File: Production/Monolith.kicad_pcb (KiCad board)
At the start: 2 copper layers, 5.7 x 10.2 mm, 276 parts, among them J102 Cell 1 NTC wires, J105 Cell 2 NTC wires, J106 Cell 3 NTC wires, J107 Cell 4 NTC wires, J108 PACK- (CELL_N), J109 CELL1 tap, J110 CELL2 tap, J111 CELL3 tap, J112 PACK+ (CELL_P_RAW), J301 TC2030-NL, J401 TYPE-C 16PCB1.6 IP68, J501 TYPE-C 16PCB1.6 IP68, Q101 AGM404AP1, Q102 AGM404AP1, Q103 AO3400A, Q104 AO3400A, Q401 PGQ04N070, Q402 PGQ04N070, Q403 AO3401A, Q404 AO3401A, Q405 AO3400A, Q406 AO3400A, Q407 PGQ04N070, Q408 PGQ04N070, Q501 PGQ04N070, Q502 PGQ04N070, Q503 AO3401A, Q504 AO3401A, Q505 AO3400A, Q506 AO3400A, Q507 PGQ04N070, Q508 PGQ04N070, U101 BQ40Z50RSMR-R2, U102 BQ294700DSGR, U204 TPS62177DQCR, U301 CC2340R5MODA, U401 TPS25751DREFR, U402 M24512-DFMC6TG, U403 BQ25756RRVR, U404 TPS62933DRLR, U405 TPD4S201TRGRRQ1, U501 TPS25751DREFR, U502 M24512-DFMC6TG, U503 BQ25756RRVR, U504 TPS62933DRLR, U505 TPD4S201TRGRRQ1

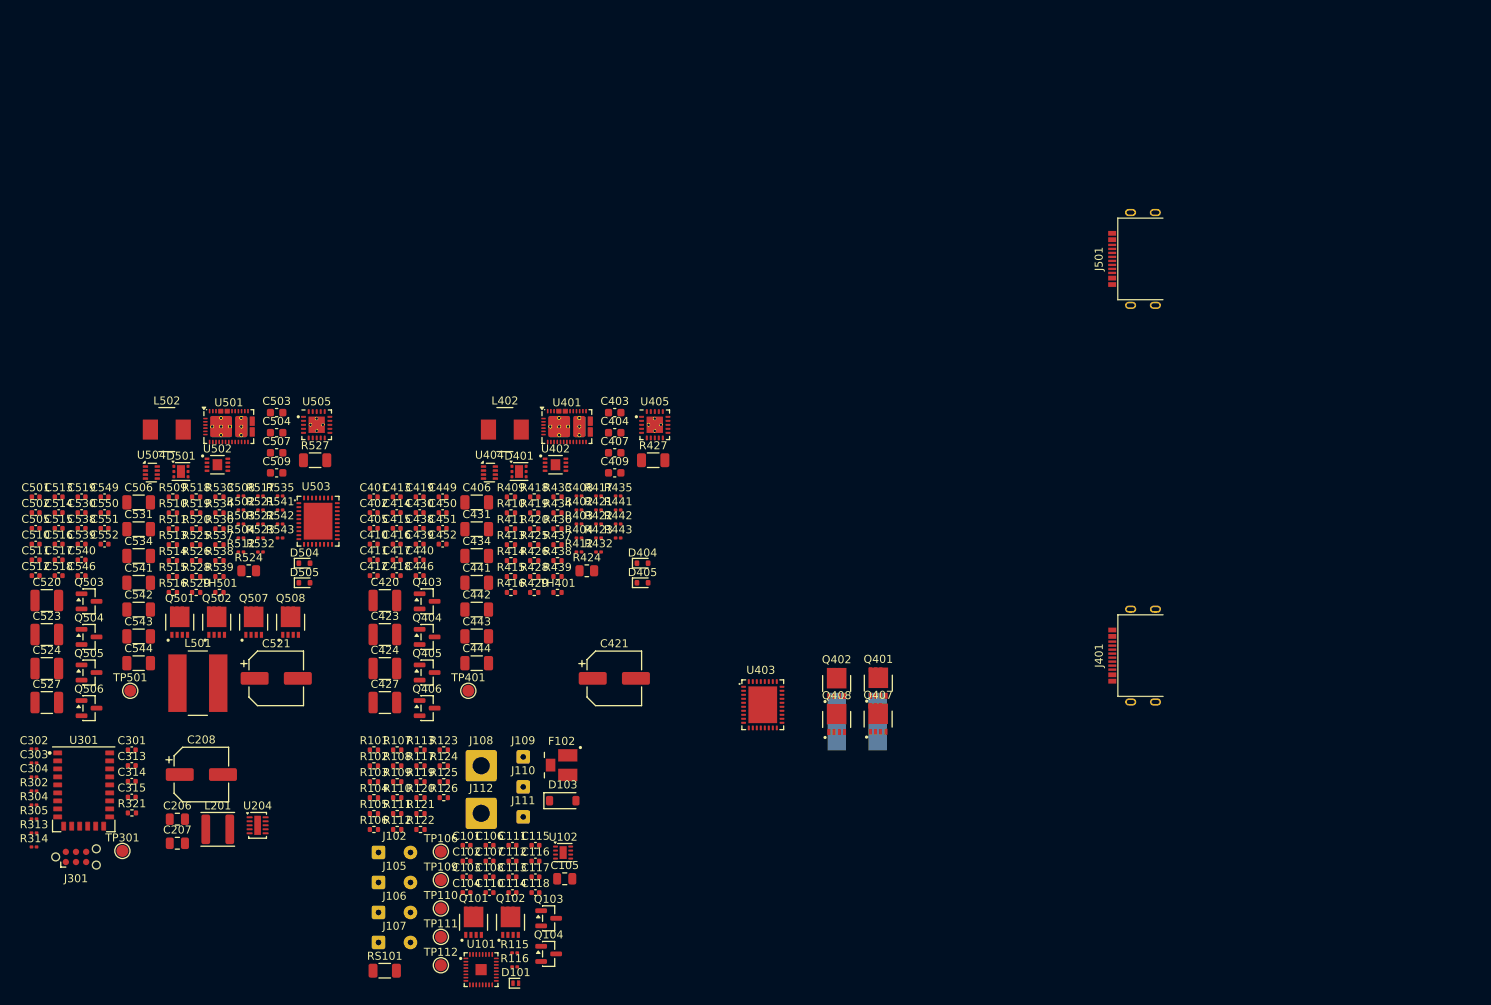
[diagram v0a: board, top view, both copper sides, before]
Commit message: Production board: 6-layer 0.8 mm stack-up, top-cap outline, pour plan
tools/make_board.py patches Monolith.kicad_pcb (footprints untouched): 6 layers,
0.8 mm, 2 oz outer / 0.5 oz inner, ENIG, filled vias; 40.5 mm R9.35 outline
from mechanical/monolith_parts.py (the bottom DXF is the end board). Via
minimum 0.35/0.2 for fan-out. J401/J501 -> TYPE-C 16PCB0.8 IP68 (C55629727).
Pour plan in Production/README.md.

Co-Authored-By: Claude Opus 5.5 <noreply@anthropic.com>
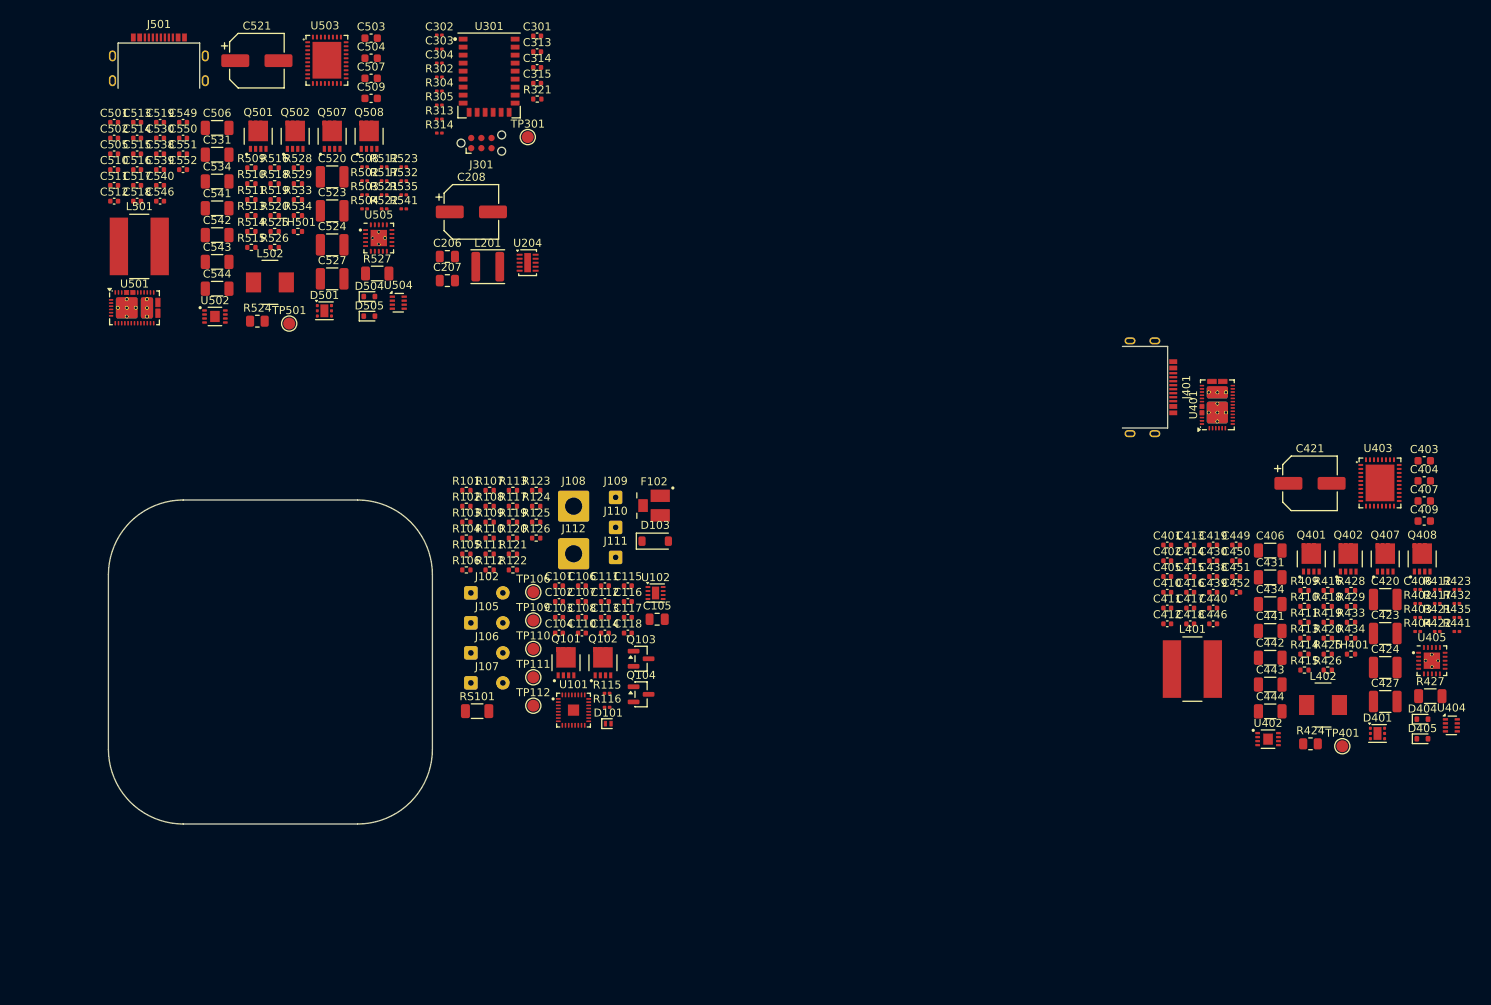
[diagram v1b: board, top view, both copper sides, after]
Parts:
- removed Q403, Q404, Q503, Q504: AO3401A, Package_TO_SOT_SMD:SOT-23
- removed Q405, Q406, Q505, Q506: AO3400A, Package_TO_SOT_SMD:SOT-23
- removed R436, R437, R536, R537: 100k, Resistor_SMD:R_0402_1005Metric
- removed R438, R439, R538, R539: 1M, Resistor_SMD:R_0402_1005Metric
- removed R442, R443, R542, R543: 100k, Resistor_SMD:R_0201_0603Metric
- L401: moved to F.Cu
- moved J501 127.3 mm to (86.1, 28.3), turned to 0 degrees
- moved C420 125.0 mm to (239.4, 92.2)
- moved C423 125.0 mm to (239.4, 96.4)
- moved C424 125.0 mm to (239.4, 100.7)
- moved C427 125.0 mm to (239.4, 104.9)
- moved U404 124.3 mm to (247.6, 107.9)
- moved D401 112.2 mm to (238.4, 108.9)
- moved TP401 109.5 mm to (234.0, 110.5)
- moved L402 107.9 mm to (231.6, 105.4)
- moved R423 107.5 mm to (248.3, 90.9)
- moved R432 107.5 mm to (248.3, 92.7)
- moved R412 107.4 mm to (245.9, 90.9)
- moved R435 105.9 mm to (248.3, 94.4)
- moved R441 105.9 mm to (248.3, 96.2)
- moved R417 105.7 mm to (245.9, 92.7)
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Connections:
- U401 pad 26: /USB Port 1/SBU1_SNS -> GND
- U401 pad 27: /USB Port 1/SBU2_SNS -> GND
- U401 pad 36: /USB Port 1/LIQ_PD -> GND
- U401 pad 37: /USB Port 1/LIQ_PU -> GND
- U405 pad 14: /USB Port 1/SBU2_SNS -> unconnected-(U405-SBU2-Pad14)
- U405 pad 15: /USB Port 1/SBU1_SNS -> unconnected-(U405-SBU1-Pad15)
- U501 pad 26: /USB Port 2/SBU1_SNS -> GND
- U501 pad 27: /USB Port 2/SBU2_SNS -> GND
- U501 pad 36: /USB Port 2/LIQ_PD -> GND
- U501 pad 37: /USB Port 2/LIQ_PU -> GND
- U505 pad 14: /USB Port 2/SBU2_SNS -> unconnected-(U505-SBU2-Pad14)
- U505 pad 15: /USB Port 2/SBU1_SNS -> unconnected-(U505-SBU1-Pad15)
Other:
- board size 5.7 x 10.2 mm -> 40.5 x 40.5 mm
- copper layers 2 -> 6

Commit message: Production board: 45.5 mm outline, J401/J501 placed on the right edge
+5 mm in x and y with R9.35 corners kept: 26.8 mm straight edge fits both
USB-C ports on one side (mechanical assembly). Outline leaves the two 10.2 mm
notch gaps; connectors at y 93.5 / 106.5, 90 deg, locked. DRC: outline closed.

Co-Authored-By: Claude Opus 5.5 <noreply@anthropic.com>
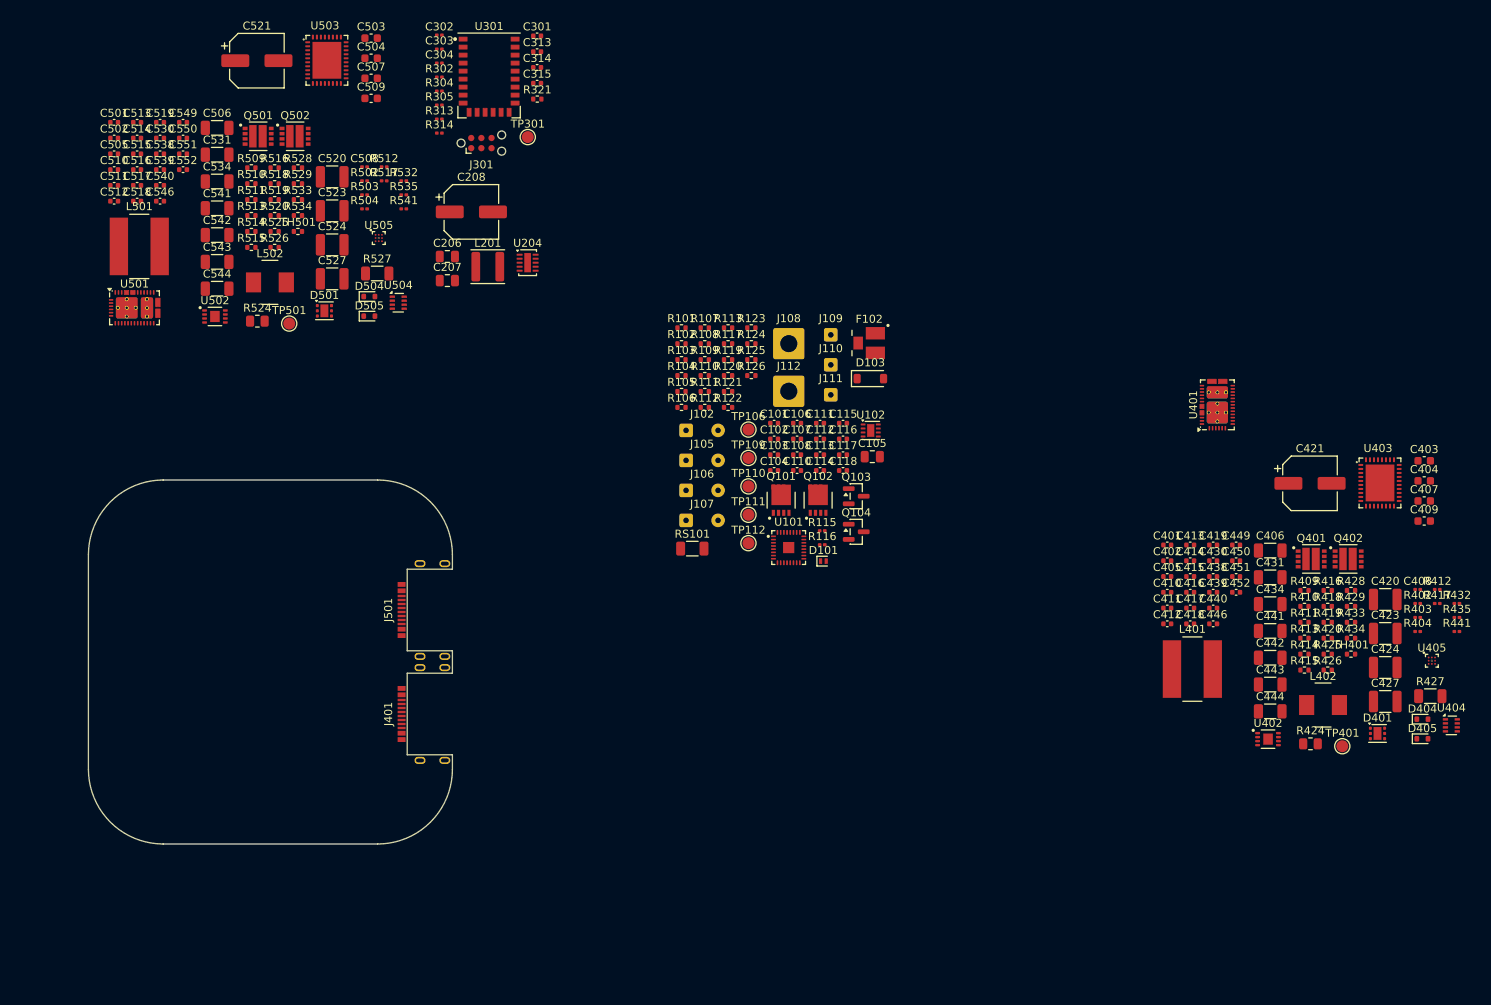
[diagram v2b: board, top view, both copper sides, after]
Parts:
- removed Q407, Q408, Q507, Q508: PGQ04N070, MonolithDev:AGM_PDFN-8_3.3x3.3mm_P0.65mm
- removed R421, R422, R423, R521, R522, R523: 10k, Resistor_SMD:R_0201_0603Metric
- J401, J501: value TYPE-C 16PCB1.6 IP68 -> TYPE-C 16PCB0.8 IP68; footprint MonolithDev:USB_C_Receptacle_ShouHan_TYPE-C_16PCB1.6_IP68 -> MonolithDev:USB_C_Receptacle_ShouHan_TYPE-C_16PCB0.8_IP68
- Q401, Q402, Q501, Q502: value PGQ04N070 -> SiZ240DT; footprint MonolithDev:AGM_PDFN-8_3.3x3.3mm_P0.65mm -> MonolithDev:Vishay_PowerPAIR_3x3S
- U405, U505: value TPD4S201TRGRRQ1 -> TPD2S300YFFR; footprint MonolithDev:TI_RGR0020C_VQFN-20-1EP_3.5x3.5mm_P0.5mm_EP2.05mm -> MonolithDev:TI_YFF0009_DSBGA-9_P0.4mm
- moved J401 93.2 mm to (122.8, 106.5), turned to 90 degrees
- moved J501 74.8 mm to (122.8, 93.5), turned to 90 degrees
- moved D103 33.7 mm to (175.0, 64.6)
- moved J109 33.7 mm to (170.0, 59.1)
- moved J110 33.7 mm to (170.0, 62.9)
- moved J111 33.7 mm to (170.0, 66.6)
- moved Q101 33.7 mm to (163.8, 79.8)
- moved Q102 33.7 mm to (168.5, 79.8)
- moved Q103 33.7 mm to (173.2, 79.3)
- moved Q104 33.7 mm to (173.2, 83.7)
- moved R123 33.7 mm to (160.1, 58.2)
- moved R124 33.7 mm to (160.1, 60.2)
- moved R126 33.7 mm to (160.1, 64.2)
- moved TP106 33.7 mm to (159.8, 70.9)
- moved TP109 33.7 mm to (159.8, 74.5)
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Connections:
- C451 pad 1: Net-(U405-VBIAS) -> /USB Port 1/VBIAS
- C551 pad 1: Net-(U505-VBIAS) -> /USB Port 2/VBIAS
- J401 pad A8: /USB Port 1/SBU1 -> unconnected-(J401-SBU1-PadA8)
- J401 pad B8: /USB Port 1/SBU2 -> unconnected-(J401-SBU2-PadB8)
- J501 pad A8: /USB Port 2/SBU1 -> unconnected-(J501-SBU1-PadA8)
- J501 pad B8: /USB Port 2/SBU2 -> unconnected-(J501-SBU2-PadB8)
- Q401 pad 1: /USB Port 1/SW1 -> /USB Port 1/HIDRV1
- Q401 pad 2: /USB Port 1/SW1 -> /USB Port 1/AC_SNS_N
- Q401 pad 3: /USB Port 1/SW1 -> /USB Port 1/AC_SNS_N
- Q401 pad 4: /USB Port 1/HIDRV1 -> /USB Port 1/AC_SNS_N
- Q401 pad 5: /USB Port 1/AC_SNS_N -> GND
- Q401 pad 6: /USB Port 1/AC_SNS_N -> GND
- Q401 pad 7: /USB Port 1/AC_SNS_N -> GND
- Q401 pad 8: /USB Port 1/AC_SNS_N -> /USB Port 1/LODRV1
- Q402 pad 1: /USB Port 1/SW2 -> /USB Port 1/HIDRV2
- Q402 pad 2: /USB Port 1/SW2 -> /USB Port 1/BAT_SNS_P
- Q402 pad 3: /USB Port 1/SW2 -> /USB Port 1/BAT_SNS_P
- Q402 pad 4: /USB Port 1/HIDRV2 -> /USB Port 1/BAT_SNS_P
- Q402 pad 5: /USB Port 1/BAT_SNS_P -> GND
- Q402 pad 6: /USB Port 1/BAT_SNS_P -> GND
- Q402 pad 7: /USB Port 1/BAT_SNS_P -> GND
- Q402 pad 8: /USB Port 1/BAT_SNS_P -> /USB Port 1/LODRV2
- Q501 pad 1: /USB Port 2/SW1 -> /USB Port 2/HIDRV1
- Q501 pad 2: /USB Port 2/SW1 -> /USB Port 2/AC_SNS_N
- Q501 pad 3: /USB Port 2/SW1 -> /USB Port 2/AC_SNS_N
- Q501 pad 4: /USB Port 2/HIDRV1 -> /USB Port 2/AC_SNS_N
- Q501 pad 5: /USB Port 2/AC_SNS_N -> GND
- Q501 pad 6: /USB Port 2/AC_SNS_N -> GND
- Q501 pad 7: /USB Port 2/AC_SNS_N -> GND
- Q501 pad 8: /USB Port 2/AC_SNS_N -> /USB Port 2/LODRV1
- Q502 pad 1: /USB Port 2/SW2 -> /USB Port 2/HIDRV2
- Q502 pad 2: /USB Port 2/SW2 -> /USB Port 2/BAT_SNS_P
- Q502 pad 3: /USB Port 2/SW2 -> /USB Port 2/BAT_SNS_P
- Q502 pad 4: /USB Port 2/HIDRV2 -> /USB Port 2/BAT_SNS_P
- Q502 pad 5: /USB Port 2/BAT_SNS_P -> GND
- Q502 pad 6: /USB Port 2/BAT_SNS_P -> GND
- Q502 pad 7: /USB Port 2/BAT_SNS_P -> GND
- Q502 pad 8: /USB Port 2/BAT_SNS_P -> /USB Port 2/LODRV2
- U403 pad 4: /USB Port 1/STAT1 -> unconnected-(U403-~{STAT1}-Pad4)
- U403 pad 5: /USB Port 1/STAT2 -> unconnected-(U403-~{STAT2}-Pad5)
- U403 pad 6: /USB Port 1/PG -> unconnected-(U403-~{PG}-Pad6)
- U503 pad 4: /USB Port 2/STAT1 -> unconnected-(U503-~{STAT1}-Pad4)
- U503 pad 5: /USB Port 2/STAT2 -> unconnected-(U503-~{STAT2}-Pad5)
- U503 pad 6: /USB Port 2/PG -> unconnected-(U503-~{PG}-Pad6)
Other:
- board size 40.5 x 40.5 mm -> 45.5 x 45.5 mm
